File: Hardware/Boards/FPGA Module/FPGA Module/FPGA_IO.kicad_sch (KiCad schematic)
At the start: 1 part, among them U1 XCKU3P-FFVA676

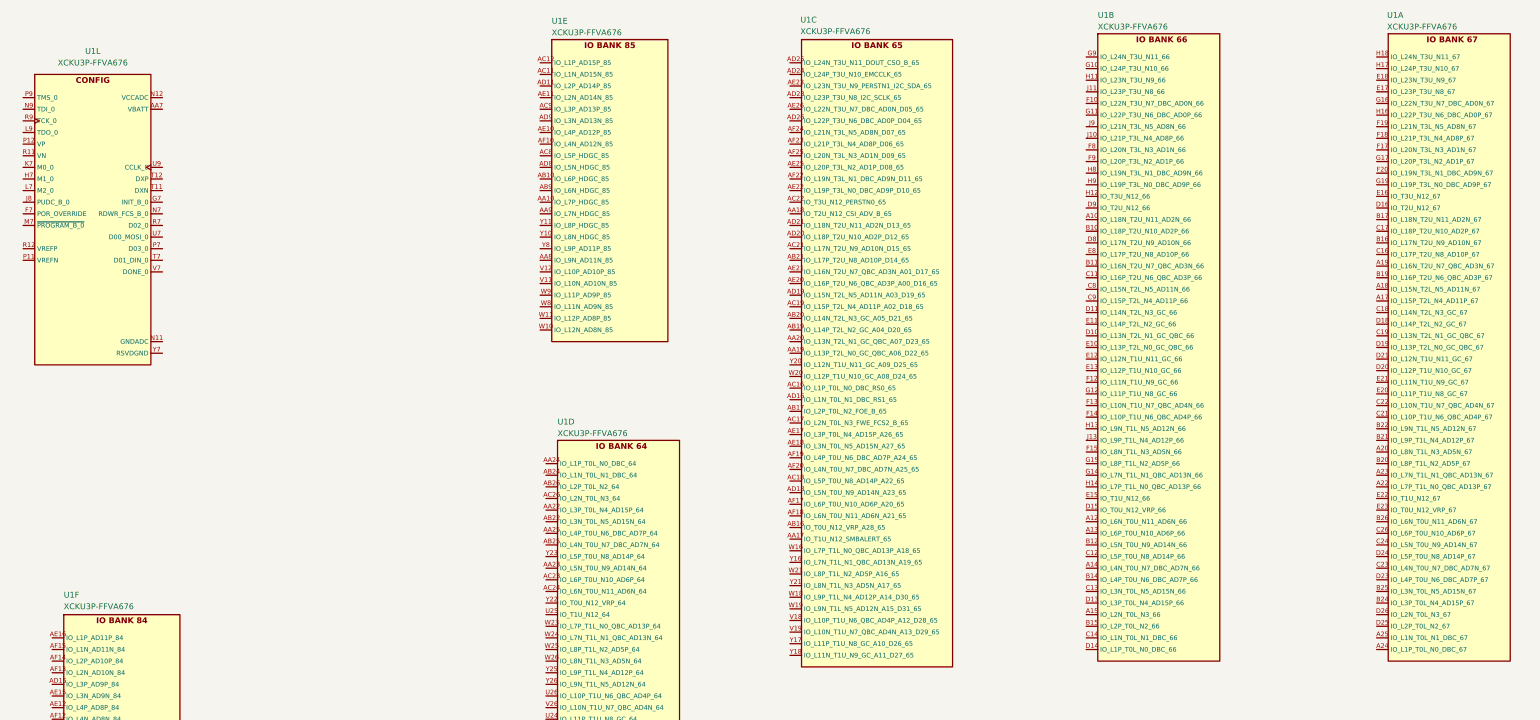
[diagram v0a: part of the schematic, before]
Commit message: Added DDR4 library
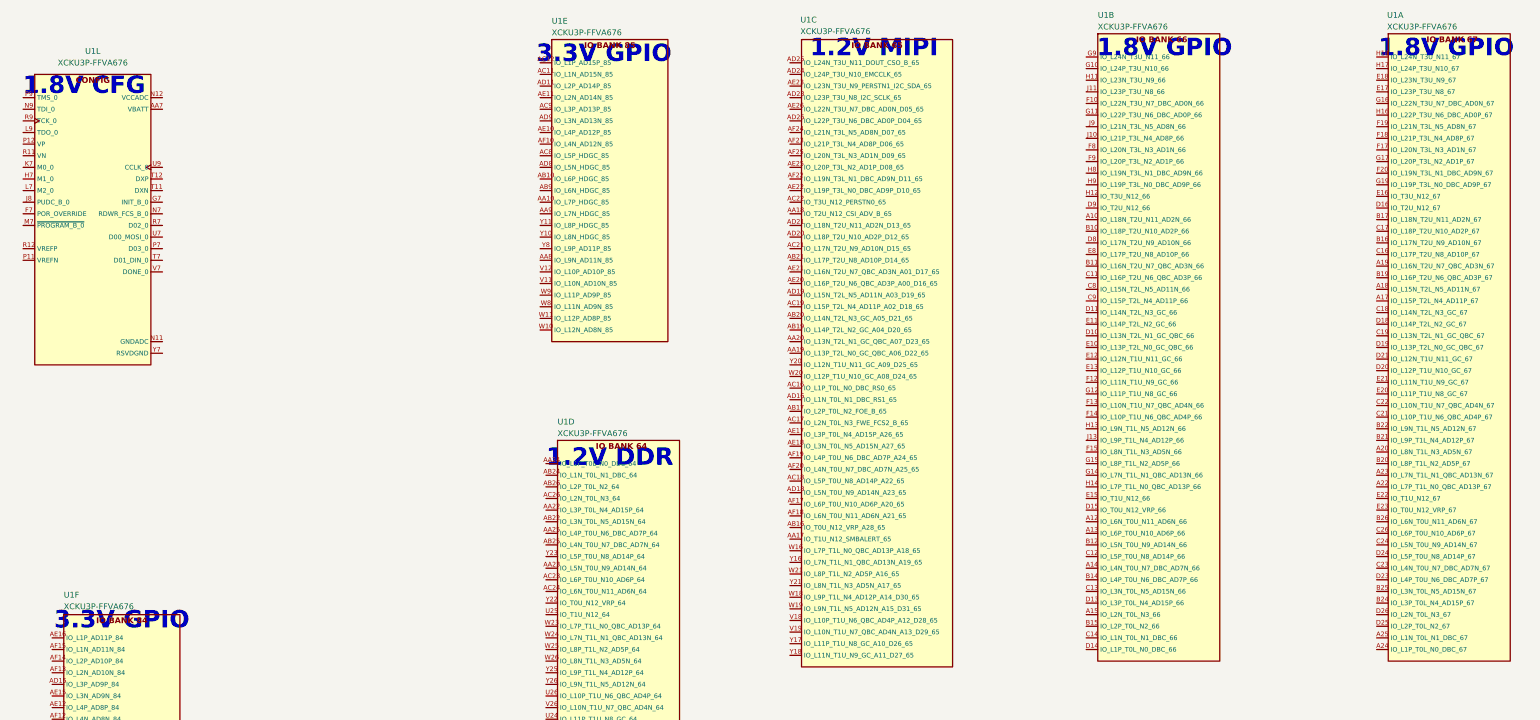
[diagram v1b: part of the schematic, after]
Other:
- note added: "1.2V DDR"
- note added: "1.2V MIPI"
- note added: "1.8V CFG"
- note added: "1.8V GPIO"
- note added: "3.3V GPIO"
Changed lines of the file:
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@@
 		(comment 1 "Designed by Michael Haahr")
+	)
+	(text "1.8V GPIO"
+		(exclude_from_sim no)
+		(at 355.6 31.115 0)
+		(effects
+			(font
+				(size 3.81 3.81)
+				(thickness 2.54)
+				(bold yes)
+				(color 255 2 2 1)
+			)
+		)
+	)
+	(text "1.2V DDR"
+		(exclude_from_sim no)
+		(at 172.72 120.65 0)
+		(effects
+			(font
+				(size 3.81 3.81)
+				(thickness 2.54)
+				(bold yes)
+				(color 255 2 2 1)
+			)
+		)
+	)
+	(text "1.8V CFG"
+		(exclude_from_sim no)
+		(at 57.785 39.37 0)
+		(effects
+			(font
+				(size 3.81 3.81)
+				(thickness 2.54)
+				(bold yes)
+				(color 255 2 2 1)
+			)
+		)
+	)
+	(text "3.3V GPIO"
+		(exclude_from_sim no)
+		(at 66.04 156.21 0)
+		(effects
+			(font
+				(size 3.81 3.81)
+				(thickness 2.54)
+				(bold yes)
+				(color 255 2 2 1)
+			)
+		)
+	)
+	(text "1.2V MIPI"
+		(exclude_from_sim no)
+		(at 230.505 31.115 0)
+		(effects
+			(font
+				(size 3.81 3.81)
+				(thickness 2.54)
+				(bold yes)
+				(color 255 2 2 1)
+			)
+		)
+	)
+	(text "3.3V GPIO"
+		(exclude_from_sim no)
+		(at 171.45 32.385 0)
+		(effects
+			(font
+				(size 3.81 3.81)
+				(thickness 2.54)
+				(bold yes)
+				(color 255 2 2 1)
+			)
+		)
+	)
+	(text "1.8V GPIO"
+		(exclude_from_sim no)
+		(at 294.005 31.115 0)
+		(effects
+			(font
+				(size 3.81 3.81)
+				(thickness 2.54)
+				(bold yes)
+				(color 255 2 2 1)
+			)
+		)
 	)
 	(symbol

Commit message: Added FPGA Config page
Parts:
- removed U1: XCKU3P-FFVA676, DICE_FPGA_Module:BGA676, symbol DICE_FPGA_Module:XCKU3P-FFVA676
- added U1: XCKU3P-FFVA676, FPGA Module:BGA676, symbol FPGA Module:XCKU3P-FFVA676
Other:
- note removed: "1.8V CFG"

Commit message: Added reference designs to Boards folder, updated FPGA IO to include DDR pins
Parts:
- added R42: 240R, Resistor_SMD:R_0402_1005Metric, symbol Device:R_US
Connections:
- net DDR_A4: now reaches U1.A17 (IO_L15P_T2L_N4_AD11P_67)
- net DDR_A5: now reaches U1.A18 (IO_L15N_T2L_N5_AD11N_67)
- net DDR_CLK_N: now reaches U1.A19 (IO_L16N_T2U_N7_QBC_AD3N_67)
- net DDR_A13: now reaches U1.A20 (IO_L8N_T1L_N3_AD5N_67)
- net DDR_A10: now reaches U1.A22 (IO_L7P_T1L_N0_QBC_AD13P_67)
- net DDR_A11: now reaches U1.A23 (IO_L7N_T1L_N1_QBC_AD13N_67)
- net DDR_CTRL_LDM_N: now reaches U1.A24 (IO_L1P_T0L_N0_DBC_67)
- net DDR_CTRL_ACT: now reaches U1.A25 (IO_L1N_T0L_N1_DBC_67)
- net DDR_A7: now reaches U1.B16 (IO_L17N_T2U_N9_AD10N_67)
- net DDR_A9: now reaches U1.B17 (IO_L18N_T2U_N11_AD2N_67)
- net DDR_CLK_P: now reaches U1.B19 (IO_L16P_T2U_N6_QBC_AD3P_67)
- net DDR_A12: now reaches U1.B20 (IO_L8P_T1L_N2_AD5P_67)
- net DDR_CTRL_WE/A14: now reaches U1.B21 (IO_L9P_T1L_N4_AD12P_67)
- net DDR_CTRL_CAS/A15: now reaches U1.B22 (IO_L9N_T1L_N5_AD12N_67)
- net DDR_D2: now reaches U1.B24 (IO_L3P_T0L_N4_AD15P_67)
- net DDR_D3: now reaches U1.B25 (IO_L3N_T0L_N5_AD15N_67)
- net DDR_D7: now reaches U1.B26 (IO_L6N_T0U_N11_AD6N_67)
- net DDR_A6: now reaches U1.C16 (IO_L17P_T2U_N8_AD10P_67)
- net DDR_A8: now reaches U1.C17 (IO_L18P_T2U_N10_AD2P_67)
- net DDR_A3: now reaches U1.C18 (IO_L14N_T2L_N3_GC_67)
- net DDR_A1: now reaches U1.C19 (IO_L13N_T2L_N1_GC_QBC_67)
- net DDR_CTRL_RAS/A16: now reaches U1.C21 (IO_L10P_T1U_N6_QBC_AD4P_67)
- net DDR_BA0: now reaches U1.C22 (IO_L10N_T1U_N7_QBC_AD4N_67)
- net DDR_CTRL_DQSL_N: now reaches U1.C23 (IO_L4N_T0U_N7_DBC_AD7N_67)
- net DDR_D5: now reaches U1.C24 (IO_L5N_T0U_N9_AD14N_67)
- net DDR_D6: now reaches U1.C26 (IO_L6P_T0U_N10_AD6P_67)
- net DDR_CTRL_ODT: now reaches U1.D16 (IO_T2U_N12_67)
- net DDR_A2: now reaches U1.D18 (IO_L14P_T2L_N2_GC_67)
- net DDR_A0: now reaches U1.D19 (IO_L13P_T2L_N0_GC_QBC_67)
- net DDR_BA1: now reaches U1.D20 (IO_L12P_T1U_N10_GC_67)
- net DDR_BG0: now reaches U1.D21 (IO_L12N_T1U_N11_GC_67)
- net DDR_CTRL_DQSL_P: now reaches U1.D23 (IO_L4P_T0U_N6_DBC_AD7P_67)
- net DDR_D4: now reaches U1.D24 (IO_L5P_T0U_N8_AD14P_67)
- net DDR_D0: now reaches U1.D25 (IO_L2P_T0L_N2_67)
- net DDR_D1: now reaches U1.D26 (IO_L2N_T0L_N3_67)
- net DDR_CTRL_CS: now reaches U1.E16 (IO_T3U_N12_67)
- net DDR_D12: now reaches U1.E17 (IO_L23P_T3U_N8_67)
- net DDR_D13: now reaches U1.E18 (IO_L23N_T3U_N9_67)
- net SYS_CLK0_P: now reaches U1.E20 (IO_L11P_T1U_N8_GC_67)
- net SYS_CLK0_N: now reaches U1.E21 (IO_L11N_T1U_N9_GC_67)
- net DDR_CTRL_CKE: now reaches U1.E22 (IO_T1U_N12_67)
- net at U1.E23 (IO_T0U_N12_VRP_67): now also R42.2
- net DDR_D9: now reaches U1.F17 (IO_L20N_T3L_N3_AD1N_67)
- net DDR_D10: now reaches U1.F18 (IO_L21P_T3L_N4_AD8P_67)
- net DDR_D11: now reaches U1.F19 (IO_L21N_T3L_N5_AD8N_67)
- net DDR_CTRL_RST: now reaches U1.F20 (IO_L19N_T3L_N1_DBC_AD9N_67)
- net DDR_CTRL_DQSU_N: now reaches U1.G16 (IO_L22N_T3U_N7_DBC_AD0N_67)
- net DDR_D8: now reaches U1.G17 (IO_L20P_T3L_N2_AD1P_67)
- net DDR_CTRL_UDM_N: now reaches U1.G19 (IO_L19P_T3L_N0_DBC_AD9P_67)
- net DDR_CTRL_DQSU_P: now reaches U1.H16 (IO_L22P_T3U_N6_DBC_AD0P_67)
- net DDR_D14: now reaches U1.H17 (IO_L24P_T3U_N10_67)
- net DDR_D15: now reaches U1.H18 (IO_L24N_T3U_N11_67)
- new net GND: R42.1
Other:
- moved on the sheet: U1A, U1B, U1C, U1D, U1E, U1F

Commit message: Using new DP to HDMI IC
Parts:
- added C110, C111, C93, C94, C95: 100nF, Capacitor_SMD:C_0402_1005Metric, symbol Device:C_Small
- added R47, R67, R77: 100R, Resistor_SMD:R_0402_1005Metric, symbol Device:R_US
- added R48: 0R, Resistor_SMD:R_0402_1005Metric, symbol Device:R_US
- added R63, R64, R65, R66, R75, R76, R78, R79: 1K, Resistor_SMD:R_0402_1005Metric, symbol Device:R_US
- added unit 7 of U1
- added U20: Si511J200, Oscillator:Oscillator_SMD_SiTime_SiT9121-6Pin_3.2x2.5mm, symbol FPGA Module:Si511
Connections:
- net GND: now also C93.2, R65.1, R66.1, R78.1, R79.1, U20.3 (GND)
- net FT600_WR: now reaches U1.AA13 (IO_L11P_AD1P_84)
- net FIFO_D10: now reaches U1.AA14 (IO_L9P_AD3P_84)
- net FIFO_D14: now reaches U1.AA15 (IO_L7P_HDGC_AD5P_84)
- net FIFO_D9: now reaches U1.AB14 (IO_L9N_AD3N_84)
- net FIFO_D13: now reaches U1.AB15 (IO_L7N_HDGC_AD5N_84)
- net FIFO_D0: now reaches U1.AC13 (IO_L5N_HDGC_AD7N_84)
- net FIFO_D1: now reaches U1.AC14 (IO_L5P_HDGC_AD7P_84)
- net FIFO_D15: now reaches U1.AD13 (IO_L6N_HDGC_AD6N_84)
- net FIFO_CLK: now reaches U1.AD14 (IO_L6P_HDGC_AD6P_84)
- net FIFO_D5: now reaches U1.AD15 (IO_L3P_AD9P_84)
- net FIFO_D3: now reaches U1.AE12 (IO_L4P_AD8P_84)
- net FIFO_D4: now reaches U1.AE15 (IO_L3N_AD9N_84)
- net FIFO_BE1: now reaches U1.AE16 (IO_L1P_AD11P_84)
- net FIFO_D2: now reaches U1.AF12 (IO_L4N_AD8N_84)
- net FIFO_D6: now reaches U1.AF13 (IO_L2N_AD10N_84)
- net FIFO_D7: now reaches U1.AF14 (IO_L2P_AD10P_84)
- net FIFO_BE0: now reaches U1.AF15 (IO_L1N_AD11N_84)
- net FT600_RD: now reaches U1.W13 (IO_L10N_AD2N_84)
- net FIFO_D8: now reaches U1.W14 (IO_L10P_AD2P_84)
- net FIFO_D12: now reaches U1.W15 (IO_L8P_HDGC_AD4P_84)
- net FIFO_D11: now reaches U1.Y15 (IO_L8N_HDGC_AD4N_84)
- net HDMI_SDA_SRC: now reaches U1.AA18 (IO_T2U_N12_CSI_ADV_B_65)
- net HDMI_CEC: now reaches U1.AC21 (IO_L17N_T2U_N9_AD10N_D15_65)
- net HDMI_HPD_SRC: now reaches U1.AC22 (IO_T3U_N12_PERSTN0_65)
- net HDMI_OE: now reaches U1.AD20 (IO_L18P_T2U_N10_AD2P_D12_65)
- net HDMI_SCL_SRC: now reaches U1.AD21 (IO_L18N_T2U_N11_AD2N_D13_65)
- net HDMI_AUX_P: now reaches U1.AD23 (IO_L23P_T3U_N8_I2C_SCLK_65)
- net UART_TX: now reaches U1.AD24 (IO_L24P_T3U_N10_EMCCLK_65)
- net UART_RX: now reaches U1.AD25 (IO_L24N_T3U_N11_DOUT_CSO_B_65)
- net HDMI_CEC_EN: now reaches U1.AD26 (IO_L22P_T3U_N6_DBC_AD0P_D04_65)
- net HDMI_I2C_EN: now reaches U1.AE22 (IO_L19P_T3L_N0_DBC_AD9P_D10_65)
- net HDMI_AUX_N: now reaches U1.AE23 (IO_L23N_T3U_N9_PERSTN1_I2C_SDA_65)
- net HDMI_PRE_SEL: now reaches U1.AE25 (IO_L20P_T3L_N2_AD1P_D08_65)
- net HDMI_SLEW_CTL: now reaches U1.AE26 (IO_L22N_T3U_N7_DBC_AD0N_D05_65)
- net HDMI_SWAP: now reaches U1.AF22 (IO_L19N_T3L_N1_DBC_AD9N_D11_65)
- net HDMI_SEL: now reaches U1.AF23 (IO_L21P_T3L_N4_AD8P_D06_65)
- net HDMI_TX_TERM_CTL: now reaches U1.AF24 (IO_L21N_T3L_N5_AD8N_D07_65)
- net HDMI_EQ_SEL: now reaches U1.AF25 (IO_L20N_T3L_N3_AD1N_D09_65)
- net SYSCLK1_P: now reaches U1.W20 (IO_L12P_T1U_N10_GC_A08_D24_65)
- net SYSCLK1_N: now reaches U1.Y20 (IO_L12N_T1U_N11_GC_A09_D25_65)
- net MBUS_D12: now reaches U1.AA10 (IO_L7P_HDGC_85)
- net CAM_PWR_EN: now reaches U1.AA8 (IO_L9N_AD11N_85)
- net MBUS_D13: now reaches U1.AA9 (IO_L7N_HDGC_85)
- net MBUS_D10: now reaches U1.AB10 (IO_L6P_HDGC_85)
- net MBUS_D11: now reaches U1.AB9 (IO_L6N_HDGC_85)
- net MBUS_D1: now reaches U1.AC11 (IO_L1N_AD15N_85)
- net MBUS_D0: now reaches U1.AC12 (IO_L1P_AD15P_85)
- net MBUS_D8: now reaches U1.AC8 (IO_L5P_HDGC_85)
- net MBUS_D4: now reaches U1.AC9 (IO_L3P_AD13P_85)
- net MBUS_D2: now reaches U1.AD11 (IO_L2P_AD14P_85)
- net MBUS_D9: now reaches U1.AD8 (IO_L5N_HDGC_85)
- net MBUS_D5: now reaches U1.AD9 (IO_L3N_AD13N_85)
- net MBUS_D6: now reaches U1.AE10 (IO_L4P_AD12P_85)
- net MBUS_D3: now reaches U1.AE11 (IO_L2N_AD14N_85)
- net MBUS_D7: now reaches U1.AF10 (IO_L4N_AD12N_85)
- net FT600_WAKEUP: now reaches U1.V11 (IO_L10N_AD10N_85)
- net CAM_LED_EN: now reaches U1.V12 (IO_L10P_AD10P_85)
- net FT600_TXE: now reaches U1.W10 (IO_L12N_AD8N_85)
- net FT600_RXE: now reaches U1.W11 (IO_L12P_AD8P_85)
- net FT600_OE: now reaches U1.W8 (IO_L11N_AD9N_85)
- net FT600_RST: now reaches U1.W9 (IO_L11P_AD9P_85)
- net FPGA_I2C_SCL: now reaches U1.Y10 (IO_L8N_HDGC_85)
- net MBUS_D14: now reaches U1.Y11 (IO_L8P_HDGC_85)
- net FPGA_I2C_SDA: now reaches U1.Y8 (IO_L9P_AD11P_85)
- net MIPI_D2_N: now reaches U1.A14 (IO_L4N_T0U_N7_DBC_AD7N_66)
- net MIPI_D1_N: now reaches U1.A15 (IO_L2N_T0L_N3_66)
- net MIPI_D3_N: now reaches U1.B12 (IO_L5N_T0U_N9_AD14N_66)
- net MIPI_D2_P: now reaches U1.B14 (IO_L4P_T0U_N6_DBC_AD7P_66)
- net MIPI_D1_P: now reaches U1.B15 (IO_L2P_T0L_N2_66)
- net MIPI_D3_P: now reaches U1.C12 (IO_L5P_T0U_N8_AD14P_66)
- net MIPI_CLK_N: now reaches U1.C13 (IO_L3N_T0L_N5_AD15N_66)
- net MIPI_D0_N: now reaches U1.C14 (IO_L1N_T0L_N1_DBC_66)
- net MIPI_CLK_P: now reaches U1.D13 (IO_L3P_T0L_N4_AD15P_66)
- net MIPI_D0_P: now reaches U1.D14 (IO_L1P_T0L_N0_DBC_66)
- net MEMCLK_N: now reaches U1.F12 (IO_L11N_T1U_N9_GC_66)
- net MEMCLK_N: now also C111.2, R76.1, R77.1, R79.2
- net MEMCLK_P: now reaches U1.G12 (IO_L11P_T1U_N8_GC_66)
- net MEMCLK_P: now also C110.2, R75.1, R77.2, R78.2
- net SYS_CLK0_N renamed SYSCLK0_N
- net SYSCLK0_N: now also C94.2, R64.1, R66.2, R67.1
- net SYS_CLK0_P renamed SYSCLK0_P
- net SYSCLK0_P: now also C95.2, R63.1, R65.2, R67.2
- new net: R47.1, R48.2, U1.AF8 (MGTAVTTRCAL_R)
- new net: R47.2, U1.AF7 (MGTRREF_R)
- new net +1V2M: R48.1, R63.2, R64.2, R75.2, R76.2
- new net +1V8: C93.1, U20.1 (OE), U20.6 (VCC)
- new net GTCLK0_N: U1.H5 (MGTREFCLK0N_227)
- new net GTCLK0_P: U1.H6 (MGTREFCLK0P_227)
- new net HDMI_CLK_N: U1.F5 (MGTREFCLK1N_227)
- new net HDMI_CLK_P: U1.F6 (MGTREFCLK1P_227)
- new net HDMI_D0_N: U1.E3 (MGTYTXN0_227)
- new net HDMI_D0_P: U1.E4 (MGTYTXP0_227)
- new net HDMI_D1_N: U1.D5 (MGTYTXN1_227)
- new net HDMI_D1_P: U1.D6 (MGTYTXP1_227)
- new net HDMI_D2_N: U1.B5 (MGTYTXN2_227)
- new net HDMI_D2_P: U1.B6 (MGTYTXP2_227)
- new net SYSCLK2_N: C111.1
- new net SYSCLK2_P: C110.1
- new net SYSCLK_C_N: C94.1, U20.5 (CLK_N)
- new net SYSCLK_C_P: C95.1, U20.4 (CLK_P)
- no-connect marks 0 -> 1
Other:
- note added: "HDMI"
- moved on the sheet: R42, U1A, U1B, U1C, U1D, U1E, U1F

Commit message: updated fpga module schematics
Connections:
- net HDMI_AUX_N is gone; now on net HDMI_SDA_SRC: U1.AE23 (IO_L23N_T3U_N9_PERSTN1_I2C_SDA_65)
- net HDMI_AUX_P is gone; now on net HDMI_SCL_SRC: U1.AD23 (IO_L23P_T3U_N8_I2C_SCLK_65)
- net HDMI_CEC_EN is gone; now on net HDMI_CEC: U1.AD26 (IO_L22P_T3U_N6_DBC_AD0P_D04_65)
- net HDMI_CLK_N is gone; now on net GTCLK1_N: U1.F5 (MGTREFCLK1N_227)
- net HDMI_CLK_P is gone; now on net GTCLK1_P: U1.F6 (MGTREFCLK1P_227)
- net HDMI_SWAP is gone; now on net HDMI_HPD_SRC: U1.AF22 (IO_L19N_T3L_N1_DBC_AD9N_D11_65)
- net HDMI_CEC: no longer U1.AC21 (IO_L17N_T2U_N9_AD10N_D15_65)
- net HDMI_EQ_SEL: now also U1.AC22 (IO_T3U_N12_PERSTN0_65); no longer U1.AF25 (IO_L20N_T3L_N3_AD1N_D09_65)
- net HDMI_HPD_SRC: no longer U1.AC22 (IO_T3U_N12_PERSTN0_65)
- net HDMI_I2C_EN: now also U1.AA18 (IO_T2U_N12_CSI_ADV_B_65); no longer U1.AE22 (IO_L19P_T3L_N0_DBC_AD9P_D10_65)
- net HDMI_OE: now also U1.AF25 (IO_L20N_T3L_N3_AD1N_D09_65); no longer U1.AD20 (IO_L18P_T2U_N10_AD2P_D12_65)
- net HDMI_PRE_SEL: now also U1.AE22 (IO_L19P_T3L_N0_DBC_AD9P_D10_65); no longer U1.AE25 (IO_L20P_T3L_N2_AD1P_D08_65)
- net HDMI_SCL_SRC: no longer U1.AD21 (IO_L18N_T2U_N11_AD2N_D13_65)
- net HDMI_SDA_SRC: no longer U1.AA18 (IO_T2U_N12_CSI_ADV_B_65)
- net HDMI_SEL: now also U1.AE25 (IO_L20P_T3L_N2_AD1P_D08_65); no longer U1.AF23 (IO_L21P_T3L_N4_AD8P_D06_65)
- net HDMI_SLEW_CTL: now also U1.AF23 (IO_L21P_T3L_N4_AD8P_D06_65); no longer U1.AE26 (IO_L22N_T3U_N7_DBC_AD0N_D05_65)
- net HDMI_LVCLK_P: now reaches U1.AA19 (IO_L13P_T2L_N0_GC_QBC_A06_D22_65)
- net HDMI_LVCLK_N: now reaches U1.AA20 (IO_L13N_T2L_N1_GC_QBC_A07_D23_65)
- net HDMI_CLK_SEL: now reaches U1.AB19 (IO_L14P_T2L_N2_GC_A04_D20_65)
- net HDMI_GTCLK_N: now reaches U1.A7 (MGTYTXN3_227)
- net HDMI_GTCLK_P: now reaches U1.A8 (MGTYTXP3_227)
- net +1V2M renamed +1V2
- net HDMI_TX_TERM_CTL renamed TPD5_EN
- new net HDMI_SDA_SRC_EN: U1.AE26 (IO_L22N_T3U_N7_DBC_AD0N_D05_65)
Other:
- moved on the sheet: C110, C111, C93, C94, C95, R63, R64, R65, R66, R67, R75, R76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
